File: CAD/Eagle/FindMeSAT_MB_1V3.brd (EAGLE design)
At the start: 99 x 49.2 mm, 136 parts, among them Q101 ABS07-32.768KHZ, Q651 ABM3B-16MHZ-10-R50-1-U, U1001 CFPT-141-20MHZ, U101 ATXMEGA256A3BU-AU, U1011 OPA354, U1021 OPA354, U1111 LM2831YMF, U1121 LM4120IM5-3.0, U201 SIM808, U301 MPU-9250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

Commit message: HW_V1.3 - Polyfuse of USB - value changed from 0.5A/1.0A to 1.1A/2.2A - some net names fixed
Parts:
- R141, R142, R162, R163, R171, R172, R173: value 68R -> 10kR
- RPOLY711: value 0.5A/1.0A -> 1.1A/2.2A
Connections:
- net CTS1: now also R223.1, U101.54; no longer R173.1, U101.55
- net DCD1: now also R222.1, U101.46; no longer R171.1, U101.47
- net DTR1: now also R171.1, U101.47; no longer R222.1, U101.46
- net RTS1: now also R173.1, U101.55; no longer R223.1, U101.54
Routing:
- net RTS1: track 100.3 -> 2.66 mm, vias 2 -> 1
- net CTS1: track 2.66 -> 100.0 mm, vias 1 -> 2
- net DTR1: track 96.4 -> 2.73 mm, vias 2 -> 0
- net DCD1: track 2.73 -> 96.4 mm, vias 0 -> 2
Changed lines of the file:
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@@
 <element name="H1203" library="holes" package="2,8-PAD" value="MOUNT-PAD-ROUND2.8" x="11.43" y="38.1" rot="R180"/>
 <element name="H1201" library="holes" package="2,8-PAD" value="MOUNT-PAD-ROUND2.8" x="94.996" y="38.1" smashed="yes" rot="R180"/>
-<element name="RPOLY711" library="rcl" package="M1206" value="0.5A/1.0A" x="96.139" y="21.463" smashed="yes" rot="MR0">
+<element name="RPOLY711" library="rcl" package="M1206" value="1.1A/2.2A" x="96.139" y="21.463" smashed="yes" rot="MR0">
 <attribute name="NAME" x="98.298" y="22.86" size="0.6096" layer="26" rot="MR0"/>
 <attribute name="VALUE" x="96.647" y="21.082" size="0.6096" layer="28" rot="MR0"/>
@@
 <attribute name="VALUE" x="32.639" y="5.842" size="0.6096" layer="28" rot="MR0"/>
 </element>
-<element name="R172" library="rcl" package="R0603" value="68R" x="80.01" y="23.114" smashed="yes">
+<element name="R172" library="rcl" package="R0603" value="10kR" x="80.01" y="23.114" smashed="yes">
 <attribute name="NAME" x="78.74" y="23.876" size="0.6096" layer="25"/>
 <attribute name="VALUE" x="79.756" y="22.733" size="0.6096" layer="27"/>
@@
 <attribute name="VALUE" x="30.48" y="32.004" size="0.6096" layer="27" rot="R90"/>
 </element>
-<element name="R173" library="rcl" package="R0603" value="68R" x="73.66" y="25.4" smashed="yes" rot="MR180">
+<element name="R173" library="rcl" package="R0603" value="10kR" x="73.66" y="25.4" smashed="yes" rot="MR180">
 <attribute name="NAME" x="74.93" y="26.289" size="0.6096" layer="26" rot="MR0"/>
 <attribute name="VALUE" x="73.914" y="25.019" size="0.6096" layer="28" rot="MR0"/>
 </element>
-<element name="R171" library="rcl" package="R0603" value="68R" x="81.28" y="20.447" smashed="yes" rot="R90">
+<element name="R171" library="rcl" package="R0603" value="10kR" x="81.28" y="20.447" smashed="yes" rot="R90">
 <attribute name="NAME" x="82.804" y="19.177" size="0.6096" layer="25" rot="R90"/>
 <attribute name="VALUE" x="81.661" y="19.939" size="0.6096" layer="27" rot="R90"/>
@@
 <attribute name="VALUE" x="39.116" y="36.449" size="0.6096" layer="28" rot="MR0"/>
 </element>
-<element name="R163" library="rcl" package="R0603" value="68R" x="82.55" y="20.32" smashed="yes" rot="MR180">
+<element name="R163" library="rcl" package="R0603" value="10kR" x="82.55" y="20.32" smashed="yes" rot="MR180">
 <attribute name="NAME" x="86.487" y="19.939" size="0.6096" layer="26" rot="MR0"/>
 <attribute name="VALUE" x="82.677" y="19.939" size="0.6096" layer="28" rot="MR0"/>
 </element>
-<element name="R162" library="rcl" package="R0603" value="68R" x="81.28" y="12.7" smashed="yes" rot="R270">
+<element name="R162" library="rcl" package="R0603" value="10kR" x="81.28" y="12.7" smashed="yes" rot="R270">
 <attribute name="NAME" x="82.804" y="11.43" size="0.6096" layer="25" rot="R90"/>
 <attribute name="VALUE" x="81.661" y="12.446" size="0.6096" layer="27" rot="R90"/>
@@
 <attribute name="VALUE" x="13.208" y="26.035" size="0.6096" layer="28" rot="MR180"/>
 </element>
-<element name="R141" library="rcl" package="R0603" value="68R" x="70.993" y="4.953" smashed="yes" rot="R180">
+<element name="R141" library="rcl" package="R0603" value="10kR" x="70.993" y="4.953" smashed="yes" rot="R180">
 <attribute name="NAME" x="67.31" y="4.699" size="0.6096" layer="25"/>
 <attribute name="VALUE" x="70.866" y="4.572" size="0.6096" layer="27"/>
 </element>
-<element name="R142" library="rcl" package="R0603" value="68R" x="70.993" y="2.921" smashed="yes" rot="R180">
+<element name="R142" library="rcl" package="R0603" value="10kR" x="70.993" y="2.921" smashed="yes" rot="R180">
 <attribute name="NAME" x="67.31" y="2.667" size="0.6096" layer="25"/>
 <attribute name="VALUE" x="70.866" y="2.54" size="0.6096" layer="27"/>
@@
 <wire x1="32.21" y1="36.528" x2="32.258" y2="36.322" width="0.1524" layer="16" curve="-90"/>
 </signal>
-<signal name="RTS1">
-<contactref element="R223" pad="1"/>
-<contactref element="U101" pad="54"/>
-<wire x1="73.1266" y1="22.987" x2="73.1266" y2="23.8506" width="0.1524" layer="1"/>
-<wire x1="73.1266" y1="23.8506" x2="73.66" y2="24.384" width="0.1524" layer="1"/>
-<wire x1="73.66" y1="24.384" x2="74.549" y2="24.384" width="0.1524" layer="1"/>
-<wire x1="74.549" y1="24.384" x2="74.93" y2="24.765" width="0.1524" layer="1"/>
-<wire x1="74.93" y1="24.765" x2="82.296" y2="24.765" width="0.1524" layer="1"/>
-<wire x1="82.296" y1="24.765" x2="85.852" y2="28.321" width="0.1524" layer="1"/>
-<wire x1="85.852" y1="28.321" x2="85.852" y2="38.608" width="0.1524" layer="1"/>
-<wire x1="85.852" y1="38.608" x2="85.725" y2="38.735" width="0.1524" layer="1"/>
-<via x="85.725" y="38.735" extent="1-16" drill="0.3048" shape="octagon"/>
-<wire x1="85.725" y1="38.735" x2="86.741" y2="37.719" width="0.1524" layer="16"/>
-<wire x1="86.741" y1="37.719" x2="90.297" y2="37.719" width="0.1524" layer="16"/>
-<wire x1="90.297" y1="37.719" x2="90.805" y2="38.227" width="0.1524" layer="16"/>
-<wire x1="90.805" y1="38.227" x2="90.805" y2="40.894" width="0.1524" layer="16"/>
-<wire x1="90.805" y1="40.894" x2="90.551" y2="41.148" width="0.1524" layer="16"/>
-<wire x1="33.401" y1="31.408" x2="33.489" y2="31.115" width="0.1524" layer="1"/>
-<wire x1="33.489" y1="31.115" x2="33.489" y2="30.392" width="0.1524" layer="1"/>
-<wire x1="33.489" y1="30.392" x2="33.782" y2="30.099" width="0.1524" layer="1"/>
-<wire x1="33.782" y1="30.099" x2="35.433" y2="30.099" width="0.1524" layer="1"/>
-<wire x1="35.433" y1="30.099" x2="41.402" y2="36.068" width="0.1524" layer="1"/>
-<wire x1="41.402" y1="36.068" x2="41.402" y2="39.751" width="0.1524" layer="1"/>
-<via x="41.402" y="39.751" extent="1-16" drill="0.3048" shape="octagon"/>
-<wire x1="41.402" y1="39.751" x2="41.402" y2="40.894" width="0.1524" layer="16"/>
-<wire x1="41.402" y1="40.894" x2="41.656" y2="41.148" width="0.1524" layer="16"/>
-<wire x1="41.656" y1="41.148" x2="90.551" y2="41.148" width="0.1524" layer="16"/>
-</signal>
 <signal name="GSM_RI">
 <contactref element="U201" pad="10"/>
@@
 <wire x1="43.18" y1="40.386" x2="89.027" y2="40.386" width="0.1524" layer="16"/>
 </signal>
-<signal name="CTS1">
+<signal name="RTS1">
 <contactref element="U101" pad="55"/>
 <contactref element="R173" pad="1"/>
@@
 <wire x1="29.337" y1="35.687" x2="29.337" y2="37.084" width="0.1524" layer="16"/>
 </signal>
-<signal name="DCD1">
+<signal name="DTR1">
 <contactref element="R171" pad="1"/>
 <contactref element="U101" pad="47"/>
@@
 <wire x1="80.303" y1="20.447" x2="78.867" y2="20.447" width="0.1524" layer="1"/>
 </signal>
-<signal name="DTR1">
+<signal name="DCD1">
 <contactref element="U101" pad="46"/>
 <contactref element="R222" pad="1"/>
@@
 </polygon>
 </signal>
+<signal name="CTS1">
+<contactref element="R223" pad="1"/>
+<contactref element="U101" pad="54"/>
+<wire x1="73.1266" y1="22.987" x2="73.1266" y2="23.8506" width="0.1524" layer="1"/>
+<wire x1="73.1266" y1="23.8506" x2="73.66" y2="24.384" width="0.1524" layer="1"/>
+<wire x1="73.66" y1="24.384" x2="74.549" y2="24.384" width="0.1524" layer="1"/>
+<wire x1="74.549" y1="24.384" x2="74.93" y2="24.765" width="0.1524" layer="1"/>
+<wire x1="74.93" y1="24.765" x2="82.296" y2="24.765" width="0.1524" layer="1"/>
+<wire x1="82.296" y1="24.765" x2="85.852" y2="28.321" width="0.1524" layer="1"/>
+<wire x1="85.852" y1="28.321" x2="85.852" y2="38.608" width="0.1524" layer="1"/>
+<wire x1="85.852" y1="38.608" x2="85.725" y2="38.735" width="0.1524" layer="1"/>
+<via x="85.725" y="38.735" extent="1-16" drill="0.3048" shape="octagon"/>
+<wire x1="85.725" y1="38.735" x2="86.741" y2="37.719" width="0.1524" layer="16"/>
+<wire x1="86.741" y1="37.719" x2="90.297" y2="37.719" width="0.1524" layer="16"/>
+<wire x1="90.297" y1="37.719" x2="90.805" y2="38.227" width="0.1524" layer="16"/>
+<wire x1="90.805" y1="38.227" x2="90.805" y2="40.894" width="0.1524" layer="16"/>
+<wire x1="90.805" y1="40.894" x2="90.551" y2="41.148" width="0.1524" layer="16"/>
+<wire x1="33.489" y1="31.115" x2="33.489" y2="30.392" width="0.1524" layer="1"/>
+<wire x1="33.489" y1="30.392" x2="33.782" y2="30.099" width="0.1524" layer="1"/>
+<wire x1="33.782" y1="30.099" x2="35.433" y2="30.099" width="0.1524" layer="1"/>
+<wire x1="35.433" y1="30.099" x2="41.402" y2="36.068" width="0.1524" layer="1"/>
+<wire x1="41.402" y1="36.068" x2="41.402" y2="39.751" width="0.1524" layer="1"/>
+<via x="41.402" y="39.751" extent="1-16" drill="0.3048" shape="octagon"/>
+<wire x1="41.402" y1="39.751" x2="41.402" y2="40.894" width="0.1524" layer="16"/>
+<wire x1="41.402" y1="40.894" x2="41.656" y2="41.148" width="0.1524" layer="16"/>
+<wire x1="41.656" y1="41.148" x2="90.551" y2="41.148" width="0.1524" layer="16"/>
+<wire x1="33.489" y1="31.115" x2="33.401" y2="31.408" width="0" layer="19" extent="1-1"/>
+</signal>
 </signals>

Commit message: HW_V1.3 - R1012: 270kR --> 330kR
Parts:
- R1012: value 270kR -> 330kR
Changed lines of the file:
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@@
 <layer number="49" name="Reference" color="7" fill="1" visible="yes" active="yes"/>
 <layer number="50" name="dxf" color="7" fill="1" visible="no" active="no"/>
-<layer number="51" name="tDocu" color="7" fill="1" visible="no" active="yes"/>
-<layer number="52" name="bDocu" color="7" fill="1" visible="no" active="yes"/>
+<layer number="51" name="tDocu" color="7" fill="1" visible="yes" active="yes"/>
+<layer number="52" name="bDocu" color="7" fill="1" visible="yes" active="yes"/>
 <layer number="53" name="tGND_GNDA" color="7" fill="9" visible="no" active="no"/>
 <layer number="54" name="bGND_GNDA" color="1" fill="9" visible="no" active="no"/>
@@
 <attribute name="VALUE" x="69.469" y="27.432" size="0.6096" layer="28" rot="MR90"/>
 </element>
-<element name="R1012" library="rcl" package="R0603" value="270kR" x="67.691" y="33.02" smashed="yes" rot="MR0">
+<element name="R1012" library="rcl" package="R0603" value="330kR" x="67.691" y="33.02" smashed="yes" rot="MR0">
 <attribute name="NAME" x="68.961" y="33.909" size="0.6096" layer="26" rot="MR0"/>
 <attribute name="VALUE" x="68.453" y="32.766" size="0.6096" layer="28" rot="MR0"/>

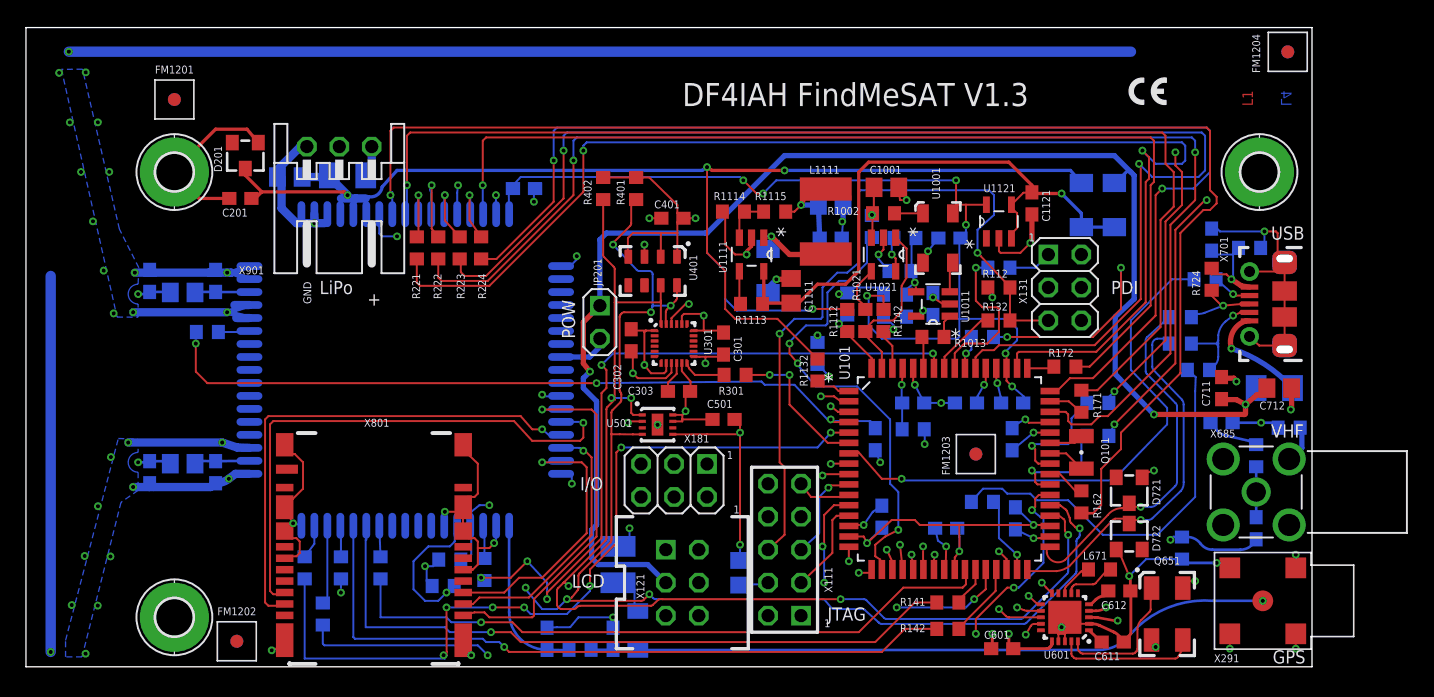
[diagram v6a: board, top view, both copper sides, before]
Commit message: HW_V1.3 - capacitor at VHF antenna added, miter applied
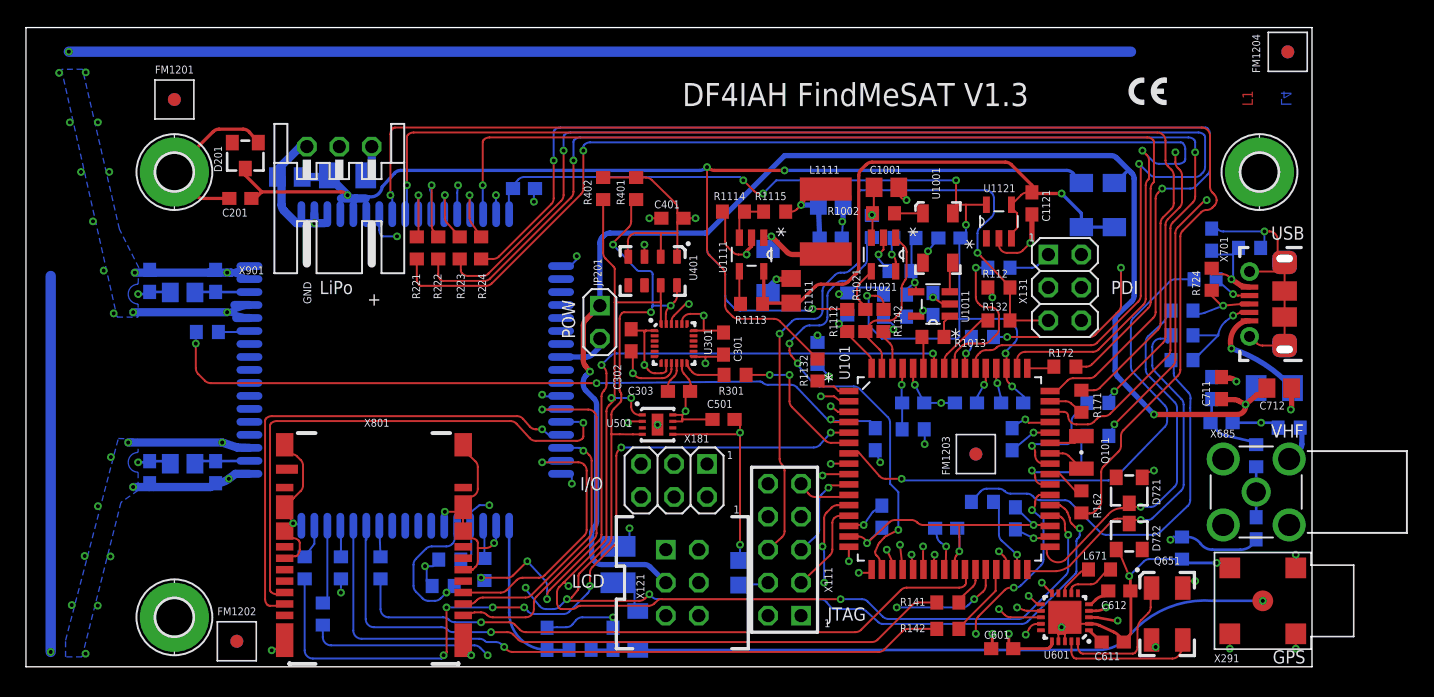
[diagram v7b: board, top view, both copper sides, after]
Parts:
- added C682: 4.7pF, rcl:C0603
- C681: value 68pF -> 33pF
- C686: value 18pF -> 4.7pF
- L681: value 150nH -> 100nH
- L682: value 68nH -> 22nH
- L686: value 150nH -> 22nH
- moved R721 1.48 mm to (89.0, 23.6)
- moved R722 0.65 mm to (89.0, 25.5)
- moved R723 0.52 mm to (89.0, 27.4)
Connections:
- net AX_ANT_I: now also C682.2
- net GND: now also C682.1
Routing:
- net AX_ANT_I: track 4.02 -> 5.87 mm
- net GSM_PWRKEY: track 106.2 -> 104.4 mm
- net +5V: track 128.4 -> 127.2 mm
- net GSM_NETLIGHT: track 63.2 -> 62.2 mm
- net GSM_STATUS: track 68.7 -> 67.8 mm
- net XO_VC_PWM: track 36.0 -> 35.1 mm
- net PDI_CLK: track 57.3 -> 56.5 mm
- net RI1: track 97.5 -> 96.7 mm
- net DCD1: track 96.4 -> 95.6 mm
- net J_D-: track 8.80 -> 8.06 mm
- net SDA1: track 107.7 -> 107.0 mm
- net SCL1: track 116.4 -> 115.7 mm
- net GSM_PCM_SYNC: track 51.5 -> 50.8 mm
- net +3V3: track 104.4 -> 103.7 mm
- net +3V0: track 77.6 -> 77.0 mm
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
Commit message: HW_V1.3 - one inductivity reversed to 150nH
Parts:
- L681: value 100nH -> 150nH
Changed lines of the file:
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@@
 <attribute name="VALUE" x="94.488" y="10.287" size="0.6096" layer="28" rot="MR90"/>
 </element>
-<element name="L681" library="rcl" package="R0603" value="100nH" x="97.282" y="18.415" smashed="yes" rot="MR180">
+<element name="L681" library="rcl" package="R0603" value="150nH" x="97.282" y="18.415" smashed="yes" rot="MR180">
 <attribute name="NAME" x="98.425" y="19.304" size="0.6096" layer="26" rot="MR0"/>
 <attribute name="VALUE" x="98.552" y="18.161" size="0.6096" layer="28" rot="MR0"/>
